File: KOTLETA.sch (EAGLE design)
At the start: 126 parts, among them CON1 CON-6P, CON2 CON-4P-JST_GH-RA, CON3 CON-4P-JST_GH-RA, IC1 STM32F105RCT6, IC2 CAT24C02, IC3 SN65HVD232D, IC4 LMR14010ADDCT, IC5 LM75BD-TSSOP8, IC6 FAN7888, IC7 ZXCT1051, IC8 3.3V, Q1 CSD18510Q5B, Q2 CSD18510Q5B, Q3 CSD18510Q5B, Q4 CSD18510Q5B, Q5 CSD18510Q5B, Q6 CSD18510Q5B, X1 24MHz

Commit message: BOM updates
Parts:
- C24, C30, C32: value 2.2nF -> 1800pF; device C_digikey:2.2NF-50V_10%_X7R-0402 -> C_digikey:1800PF-50V_10%_X7R-0402
- R13, R18, R22: value 3K9 -> 4K7; device R_digikey:3K9-1%-0402 -> R_digikey:4K7-1%-0402
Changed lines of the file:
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@@
 <part name="C25" library="C_digikey" library_urn="urn:adsk.eagle:library:2539367" deviceset="22µF" device="-1206" package3d_urn="urn:adsk.eagle:package:2539382/2" technology="-35V_20%_X5R" value="22µF"/>
 <part name="C26" library="C_digikey" library_urn="urn:adsk.eagle:library:2539367" deviceset="22µF" device="-1206" package3d_urn="urn:adsk.eagle:package:2539382/2" technology="-35V_20%_X5R" value="22µF"/>
-<part name="C24" library="C_digikey" library_urn="urn:adsk.eagle:library:2539367" deviceset="2.2NF" device="-0402" package3d_urn="urn:adsk.eagle:package:2539379/2" technology="-50V_10%_X7R" value="2.2nF"/>
-<part name="R13" library="R_digikey" library_urn="urn:adsk.eagle:library:2539499" deviceset="3K9" device="-0402" package3d_urn="urn:adsk.eagle:package:2539512/2" technology="-1%" value="3K9"/>
+<part name="C24" library="C_digikey" library_urn="urn:adsk.eagle:library:2539367" deviceset="1800PF" device="-0402" package3d_urn="urn:adsk.eagle:package:2539379/2" technology="-50V_10%_X7R" value="1800pF"/>
+<part name="R13" library="R_digikey" library_urn="urn:adsk.eagle:library:2539499" deviceset="4K7" device="-0402" package3d_urn="urn:adsk.eagle:package:2539512/2" technology="-1%" value="4K7"/>
 <part name="R10" library="R_digikey" library_urn="urn:adsk.eagle:library:2539499" deviceset="560R" device="-0402" package3d_urn="urn:adsk.eagle:package:2539512/2" technology="-1%" value="560R"/>
 <part name="Q1" library="mosfet" library_urn="urn:adsk.eagle:library:2640523" deviceset="CSD18510Q5B" device="" package3d_urn="urn:adsk.eagle:package:1040149/4"/>
@@
 <part name="R12" library="R_digikey" library_urn="urn:adsk.eagle:library:2539499" deviceset="3R" device="-0402" package3d_urn="urn:adsk.eagle:package:2539512/2" technology="-5%" value="3R"/>
 <part name="R11" library="R_digikey" library_urn="urn:adsk.eagle:library:2539499" deviceset="3R" device="-0402" package3d_urn="urn:adsk.eagle:package:2539512/2" technology="-5%" value="3R"/>
-<part name="C30" library="C_digikey" library_urn="urn:adsk.eagle:library:2539367" deviceset="2.2NF" device="-0402" package3d_urn="urn:adsk.eagle:package:2539379/2" technology="-50V_10%_X7R" value="2.2nF"/>
-<part name="R18" library="R_digikey" library_urn="urn:adsk.eagle:library:2539499" deviceset="3K9" device="-0402" package3d_urn="urn:adsk.eagle:package:2539512/2" technology="-1%" value="3K9"/>
+<part name="C30" library="C_digikey" library_urn="urn:adsk.eagle:library:2539367" deviceset="1800PF" device="-0402" package3d_urn="urn:adsk.eagle:package:2539379/2" technology="-50V_10%_X7R" value="1800pF"/>
+<part name="R18" library="R_digikey" library_urn="urn:adsk.eagle:library:2539499" deviceset="4K7" device="-0402" package3d_urn="urn:adsk.eagle:package:2539512/2" technology="-1%" value="4K7"/>
 <part name="R15" library="R_digikey" library_urn="urn:adsk.eagle:library:2539499" deviceset="560R" device="-0402" package3d_urn="urn:adsk.eagle:package:2539512/2" technology="-1%" value="560R"/>
 <part name="Q3" library="mosfet" library_urn="urn:adsk.eagle:library:2640523" deviceset="CSD18510Q5B" device="" package3d_urn="urn:adsk.eagle:package:1040149/4"/>
@@
 <part name="R17" library="R_digikey" library_urn="urn:adsk.eagle:library:2539499" deviceset="3R" device="-0402" package3d_urn="urn:adsk.eagle:package:2539512/2" technology="-5%" value="3R"/>
 <part name="R16" library="R_digikey" library_urn="urn:adsk.eagle:library:2539499" deviceset="3R" device="-0402" package3d_urn="urn:adsk.eagle:package:2539512/2" technology="-5%" value="3R"/>
-<part name="C32" library="C_digikey" library_urn="urn:adsk.eagle:library:2539367" deviceset="2.2NF" device="-0402" package3d_urn="urn:adsk.eagle:package:2539379/2" technology="-50V_10%_X7R" value="2.2nF"/>
-<part name="R22" library="R_digikey" library_urn="urn:adsk.eagle:library:2539499" deviceset="3K9" device="-0402" package3d_urn="urn:adsk.eagle:package:2539512/2" technology="-1%" value="3K9"/>
+<part name="C32" library="C_digikey" library_urn="urn:adsk.eagle:library:2539367" deviceset="1800PF" device="-0402" package3d_urn="urn:adsk.eagle:package:2539379/2" technology="-50V_10%_X7R" value="1800pF"/>
+<part name="R22" library="R_digikey" library_urn="urn:adsk.eagle:library:2539499" deviceset="4K7" device="-0402" package3d_urn="urn:adsk.eagle:package:2539512/2" technology="-1%" value="4K7"/>
 <part name="R19" library="R_digikey" library_urn="urn:adsk.eagle:library:2539499" deviceset="560R" device="-0402" package3d_urn="urn:adsk.eagle:package:2539512/2" technology="-1%" value="560R"/>
 <part name="Q5" library="mosfet" library_urn="urn:adsk.eagle:library:2640523" deviceset="CSD18510Q5B" device="" package3d_urn="urn:adsk.eagle:package:1040149/4"/>

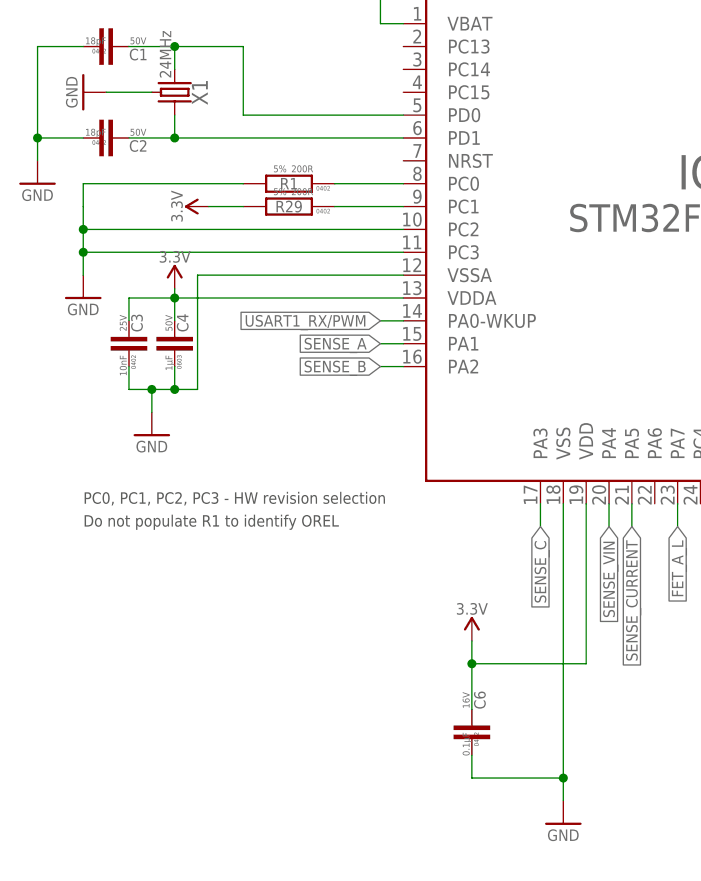
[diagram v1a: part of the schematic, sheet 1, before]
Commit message: Its 10V5 noew. HW ID stuff also fixed
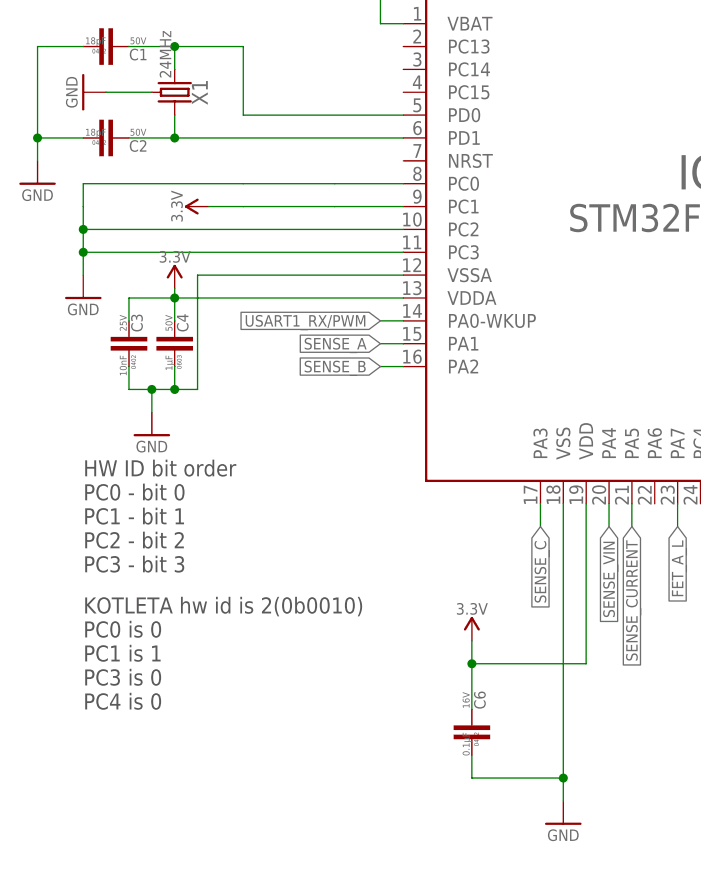
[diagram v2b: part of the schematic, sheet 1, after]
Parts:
- removed R1, R29: 200R, R_digikey:200R-5%-0402
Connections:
- removed net N$15: IC1.PC1, R29.1
- removed net N$9: IC1.PC0, R1.1
- net GND: now also IC1.PC0; no longer R1.2
- net VDD_3V3: now also IC1.PC1; no longer R29.2
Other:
- note added: "HW ID bit order PC0 - bit 0 PC1 - bit 1 PC2 - bit 2 PC3 - bit 3"
- note added: "KOTLETA hw id is 2(0b0010) PC0 is 0 PC1 is 1 PC3 is 0 PC4 is 0"
- note removed: "Do not populate R1 to identify OREL"
- note removed: "PC0, PC1, PC2, PC3 - HW revision selection"
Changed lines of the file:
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@@
 <variant name="basic" populate="no"/>
 </part>
-<part name="R1" library="R_digikey" library_urn="urn:adsk.eagle:library:2539499" deviceset="200R" device="-0402" package3d_urn="urn:adsk.eagle:package:2539512/2" technology="-5%" value="200R"/>
 <part name="R26" library="R_digikey" library_urn="urn:adsk.eagle:library:2539499" deviceset="200R" device="-0402" package3d_urn="urn:adsk.eagle:package:2539512/2" technology="-5%" value="200R">
 <attribute name="PARTNO" value="RC0402FR-07240RL"/>
@@
 <part name="GND14" library="sapog_reference_hardware" deviceset="GND" device=""/>
 <part name="C12" library="C_digikey" library_urn="urn:adsk.eagle:library:2539367" deviceset="0.1µF" device="-0402" package3d_urn="urn:adsk.eagle:package:2539379/2" technology="-16V_10%_X7R" value="0.1µF"/>
-<part name="+P1" library="supply_symbols" library_urn="urn:adsk.eagle:library:5017758" deviceset="9V" device=""/>
+<part name="+P1" library="supply_symbols" library_urn="urn:adsk.eagle:library:5017758" deviceset="10V5" device=""/>
 <part name="+P2" library="supply_symbols" library_urn="urn:adsk.eagle:library:5017758" deviceset="VBAT" device=""/>
 <part name="+P3" library="supply_symbols" library_urn="urn:adsk.eagle:library:5017758" deviceset="VBAT" device=""/>
@@
 <part name="C38" library="C_digikey" library_urn="urn:adsk.eagle:library:2539367" deviceset="22µF" device="-1206" package3d_urn="urn:adsk.eagle:package:2539382/2" technology="-35V_20%_X5R" value="22µF"/>
 <part name="GND33" library="sapog_reference_hardware" deviceset="GND" device=""/>
-<part name="+P12" library="supply_symbols" library_urn="urn:adsk.eagle:library:5017758" deviceset="9V" device=""/>
+<part name="+P12" library="supply_symbols" library_urn="urn:adsk.eagle:library:5017758" deviceset="10V5" device=""/>
 <part name="R14" library="SHUNT_RESISTORS" library_urn="urn:adsk.eagle:library:2644450" deviceset="CURRENT_SHUNT_KELVIN" device="-2010-KELVIN" package3d_urn="urn:adsk.eagle:package:8637302/2" technology="-0.001R" value="0.001R"/>
 <part name="PAD1" library="PADS" library_urn="urn:adsk.eagle:library:3188696" deviceset="PAD" device="-HOLE-0.6" package3d_urn="urn:adsk.eagle:package:6513718/2" value="PAD-HOLE-0.6">
@@
 <variant name="basic" populate="no"/>
 </part>
-<part name="R29" library="R_digikey" library_urn="urn:adsk.eagle:library:2539499" deviceset="200R" device="-0402" package3d_urn="urn:adsk.eagle:package:2539512/2" technology="-5%" value="200R"/>
 <part name="P+12" library="sapog_reference_hardware" deviceset="3.3V" device=""/>
 <part name="R30" library="R_digikey" library_urn="urn:adsk.eagle:library:2539499" deviceset="10K" device="-0402" package3d_urn="urn:adsk.eagle:package:2539512/2" technology="-0.1%" value="10K"/>
@@
 <wire x1="182.88" y1="63.5" x2="254" y2="63.5" width="0.1524" layer="97" style="shortdash"/>
 <wire x1="254" y1="63.5" x2="254" y2="116.84" width="0.1524" layer="97" style="shortdash"/>
-<text x="17.78" y="66.04" size="1.27" layer="97" font="vector" ratio="15">PC0, PC1, PC2, PC3 - HW revision selection</text>
-<text x="17.78" y="63.5" size="1.27" layer="97" font="vector" ratio="15">Do not populate R1 to identify OREL</text>
 <wire x1="160.02" y1="167.64" x2="160.02" y2="132.08" width="0.1524" layer="97" style="shortdash"/>
 <wire x1="160.02" y1="132.08" x2="205.74" y2="132.08" width="0.1524" layer="97" style="shortdash"/>
@@
 <text x="139.7" y="63.5" size="1.27" layer="97" font="vector">Place R26 TO WRITE PROTECT</text>
 <text x="139.7" y="40.64" size="1.778" layer="97">WP pin pull up is optional</text>
+<text x="17.78" y="58.42" size="1.778" layer="97">HW ID bit order
+PC0 - bit 0
+PC1 - bit 1
+PC2 - bit 2
+PC3 - bit 3</text>
+<text x="17.78" y="43.18" size="1.778" layer="97">KOTLETA hw id is 2(0b0010)
+PC0 is 0
+PC1 is 1
+PC3 is 0
+PC4 is 0</text>
 </plain>
 <instances>
@@
 <instance part="FD3" gate="G$1" x="134.62" y="10.16" smashed="yes"/>
 <instance part="FD4" gate="G$1" x="124.46" y="10.16" smashed="yes"/>
-<instance part="R1" gate="G$1" x="40.64" y="101.6" smashed="yes" rot="R180">
-<attribute name="NAME" x="40.64" y="101.6" size="1.27" layer="95" rot="R180" align="center"/>
-<attribute name="VALUE" x="40.894" y="103.632" size="0.762" layer="96" rot="R180" align="bottom-right"/>
-<attribute name="PACKAGE" x="44.45" y="101.092" size="0.508" layer="95" rot="R180" align="center"/>
-<attribute name="TOLERANCE" x="40.386" y="103.632" size="0.762" layer="96" rot="R180"/>
-</instance>
 <instance part="R26" gate="G$1" x="172.72" y="66.04" smashed="yes" rot="R270">
 <attribute name="PARTNO" x="172.72" y="66.04" size="1.778" layer="96" rot="R270" display="off"/>
@@
 <instance part="PAD16" gate="G$1" x="248.92" y="119.38" smashed="yes" rot="MR0">
 <attribute name="NAME" x="248.92" y="120.65" size="1.27" layer="95" font="vector" ratio="15" rot="MR0" align="center"/>
-</instance>
-<instance part="R29" gate="G$1" x="40.64" y="99.06" smashed="yes" rot="R180">
-<attribute name="NAME" x="40.64" y="99.06" size="1.27" layer="95" rot="R180" align="center"/>
-<attribute name="VALUE" x="40.894" y="101.092" size="0.762" layer="96" rot="R180" align="bottom-right"/>
-<attribute name="PACKAGE" x="44.45" y="98.552" size="0.508" layer="95" rot="R180" align="center"/>
-<attribute name="TOLERANCE" x="40.386" y="101.092" size="0.762" layer="96" rot="R180"/>
 </instance>
 <instance part="P+12" gate="G$1" x="31.75" y="99.06" smashed="yes" rot="R90">
@@
 <wire x1="35.56" y1="101.6" x2="17.78" y2="101.6" width="0.1524" layer="91"/>
 <wire x1="17.78" y1="101.6" x2="17.78" y2="99.06" width="0.1524" layer="91"/>
-<pinref part="R1" gate="G$1" pin="2"/>
+<pinref part="IC1" gate="G$1" pin="PC0"/>
+<wire x1="53.34" y1="101.6" x2="45.72" y2="101.6" width="0.1524" layer="91"/>
+<wire x1="45.72" y1="101.6" x2="35.56" y2="101.6" width="0.1524" layer="91"/>
 </segment>
 <segment>
@@
 </segment>
 <segment>
-<pinref part="R29" gate="G$1" pin="2"/>
 <pinref part="P+12" gate="G$1" pin="VDD_3V3"/>
 <wire x1="35.56" y1="99.06" x2="31.75" y2="99.06" width="0.1524" layer="91"/>
+<pinref part="IC1" gate="G$1" pin="PC1"/>
+<wire x1="53.34" y1="99.06" x2="45.72" y2="99.06" width="0.1524" layer="91"/>
+<wire x1="45.72" y1="99.06" x2="35.56" y2="99.06" width="0.1524" layer="91"/>
 </segment>
 </net>
@@
 <pinref part="R25" gate="G$1" pin="1"/>
 <wire x1="137.16" y1="91.44" x2="147.32" y2="91.44" width="0.1524" layer="91"/>
-</segment>
-</net>
-<net name="N$9" class="0">
-<segment>
-<pinref part="IC1" gate="G$1" pin="PC0"/>
-<wire x1="53.34" y1="101.6" x2="45.72" y2="101.6" width="0.1524" layer="91"/>
-<pinref part="R1" gate="G$1" pin="1"/>
 </segment>
 </net>
@@
 <pinref part="IC1" gate="G$1" pin="PC11"/>
 <wire x1="99.06" y1="147.32" x2="99.06" y2="134.62" width="0.1524" layer="91"/>
-</segment>
-</net>
-<net name="N$15" class="0">
-<segment>
-<pinref part="IC1" gate="G$1" pin="PC1"/>
-<pinref part="R29" gate="G$1" pin="1"/>
-<wire x1="53.34" y1="99.06" x2="45.72" y2="99.06" width="0.1524" layer="91"/>
 </segment>
 </net>
@@
 <wire x1="139.7" y1="83.82" x2="139.7" y2="86.36" width="0.1524" layer="91"/>
 <junction x="139.7" y="86.36"/>
-<pinref part="+P1" gate="G$1" pin="VDD_9V"/>
+<pinref part="+P1" gate="G$1" pin="VDD_10V5"/>
 <wire x1="139.7" y1="86.36" x2="139.7" y2="88.9" width="0.1524" layer="91"/>
 <pinref part="C36" gate="G$1" pin="1"/>
@@
 <wire x1="25.4" y1="121.92" x2="25.4" y2="119.38" width="0.1524" layer="91"/>
 <junction x="25.4" y="119.38"/>
-<pinref part="+P12" gate="G$1" pin="VDD_9V"/>
-</segment>
-</net>
+<pinref part="+P12" gate="G$1" pin="VDD_10V5"/>
+</segment>
+</net>

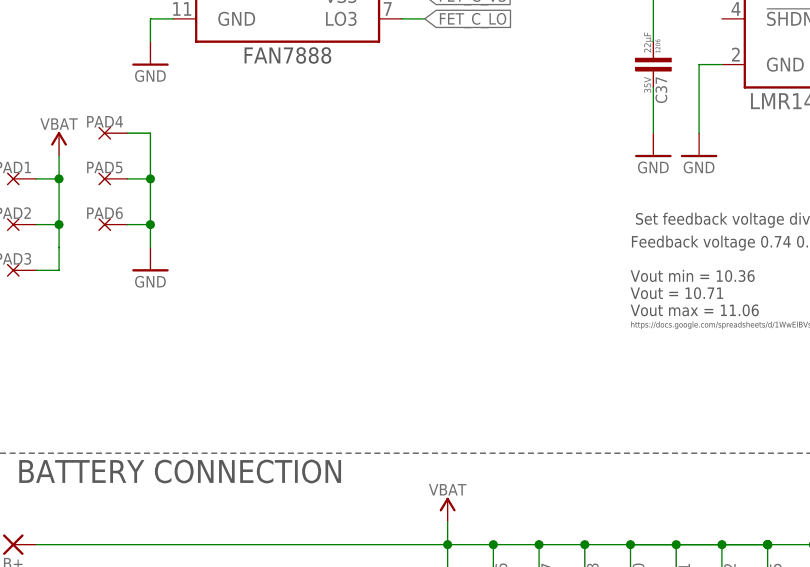
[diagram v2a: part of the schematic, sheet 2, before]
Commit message: pads for bulk capacitor
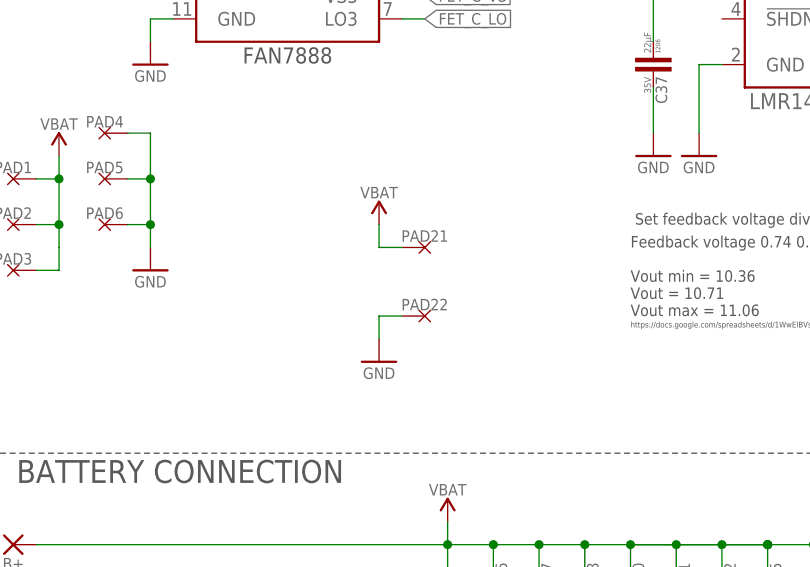
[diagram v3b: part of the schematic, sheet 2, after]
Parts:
- added PAD21, PAD22: PAD-HOLE-0.8, PADS:PAD-HOLE-0.8
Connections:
- net GND: now also PAD22.P$1
- net VBAT: now also PAD21.P$1
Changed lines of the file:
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@@
 </attributes>
 <variantdefs>
-<variantdef name="basic" current="yes"/>
+<variantdef name="basic"/>
 </variantdefs>
 <classes>
@@
 <part name="P+12" library="sapog_reference_hardware" deviceset="3.3V" device=""/>
 <part name="R30" library="R_digikey" library_urn="urn:adsk.eagle:library:2539499" deviceset="10K" device="-0402" package3d_urn="urn:adsk.eagle:package:2539512/2" technology="-0.1%" value="10K"/>
+<part name="PAD21" library="PADS" library_urn="urn:adsk.eagle:library:3188696" deviceset="PAD" device="-HOLE-0.8"/>
+<part name="PAD22" library="PADS" library_urn="urn:adsk.eagle:library:3188696" deviceset="PAD" device="-HOLE-0.8"/>
+<part name="+P13" library="supply_symbols" library_urn="urn:adsk.eagle:library:5017758" deviceset="VBAT" device=""/>
+<part name="GND46" library="sapog_reference_hardware" deviceset="GND" device=""/>
 </parts>
 <sheets>
@@
 <attribute name="TOLERANCE" x="141.732" y="63.754" size="0.762" layer="96" rot="R90"/>
 </instance>
+<instance part="PAD21" gate="G$1" x="55.88" y="60.96" smashed="yes" rot="MR0">
+<attribute name="NAME" x="55.88" y="62.23" size="1.27" layer="95" font="vector" ratio="15" rot="MR0" align="center"/>
+</instance>
+<instance part="PAD22" gate="G$1" x="55.88" y="53.34" smashed="yes" rot="MR0">
+<attribute name="NAME" x="55.88" y="54.61" size="1.27" layer="95" font="vector" ratio="15" rot="MR0" align="center"/>
+</instance>
+<instance part="+P13" gate="G$1" x="50.8" y="63.5" smashed="yes">
+<attribute name="VALUE" x="50.8" y="67.056" size="1.27" layer="96" font="vector" ratio="15" align="center"/>
+</instance>
+<instance part="GND46" gate="1" x="50.8" y="48.26" smashed="yes">
+<attribute name="VALUE" x="50.8" y="46.99" size="1.27" layer="96" font="vector" ratio="15" align="center"/>
+</instance>
 </instances>
 <busses>
@@
 <pinref part="GND16" gate="1" pin="GND"/>
 <wire x1="139.7" y1="58.42" x2="139.7" y2="55.88" width="0.1524" layer="91"/>
+</segment>
+<segment>
+<pinref part="PAD22" gate="G$1" pin="P$1"/>
+<wire x1="53.34" y1="53.34" x2="50.8" y2="53.34" width="0.1524" layer="91"/>
+<pinref part="GND46" gate="1" pin="GND"/>
+<wire x1="50.8" y1="53.34" x2="50.8" y2="50.8" width="0.1524" layer="91"/>
 </segment>
 </net>
@@
 <junction x="15.24" y="68.58"/>
 </segment>
-</net>
+<segment>
+<pinref part="PAD21" gate="G$1" pin="P$1"/>
+<wire x1="53.34" y1="60.96" x2="50.8" y2="60.96" width="0.1524" layer="91"/>
+<pinref part="+P13" gate="G$1" pin="VBAT"/>
+<wire x1="50.8" y1="60.96" x2="50.8" y2="63.5" width="0.1524" layer="91"/>
+</segment>
+</net>
